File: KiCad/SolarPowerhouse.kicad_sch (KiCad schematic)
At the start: 0 parts

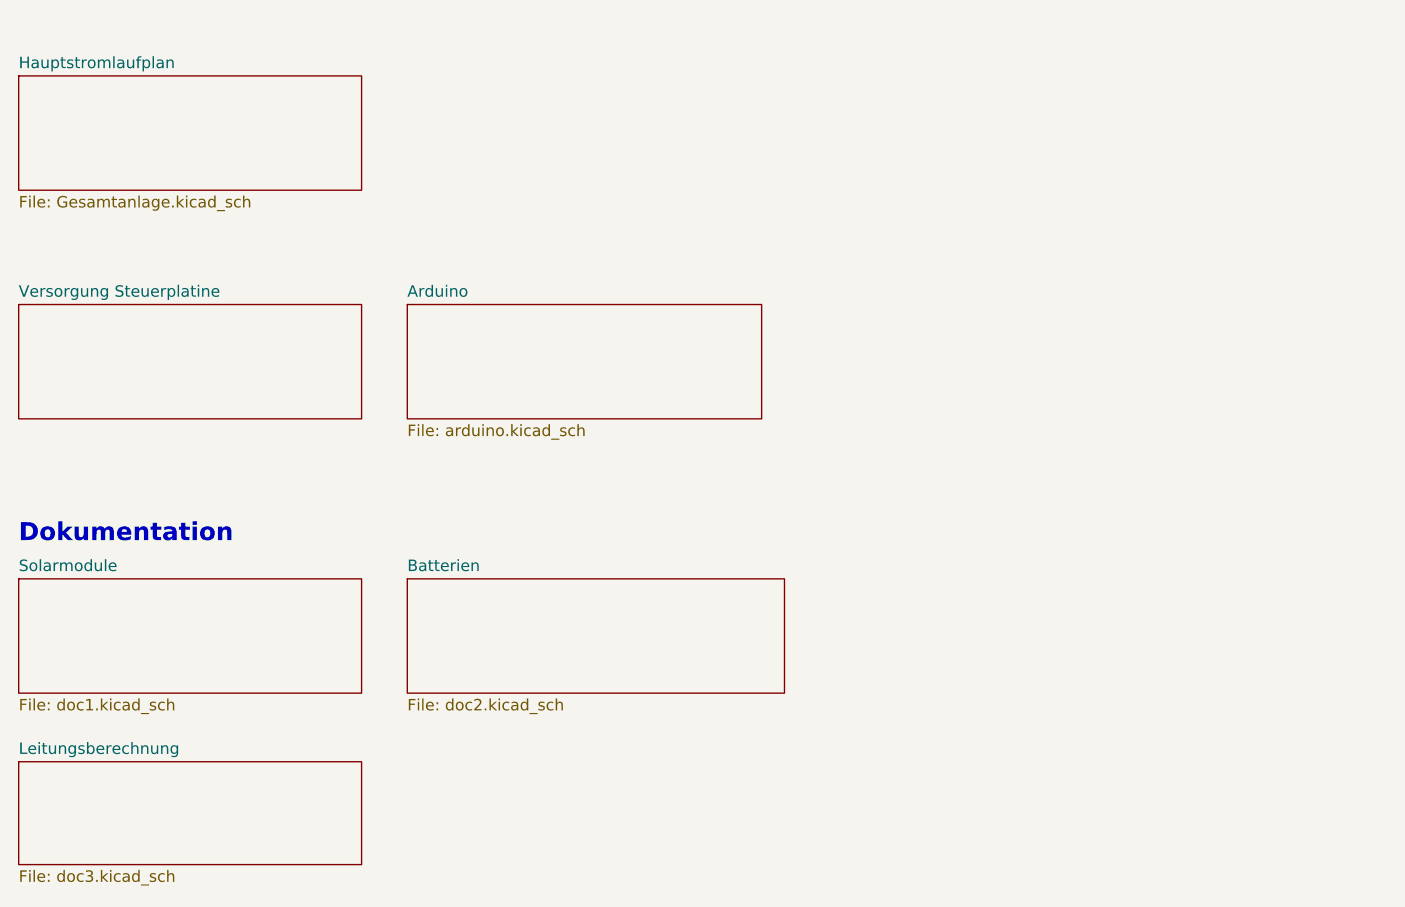
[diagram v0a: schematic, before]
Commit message: repository clean up | circuit diagram modified -> still have to add the wiring of the power supply in the circuit cabinet and the wiring of the UPS module
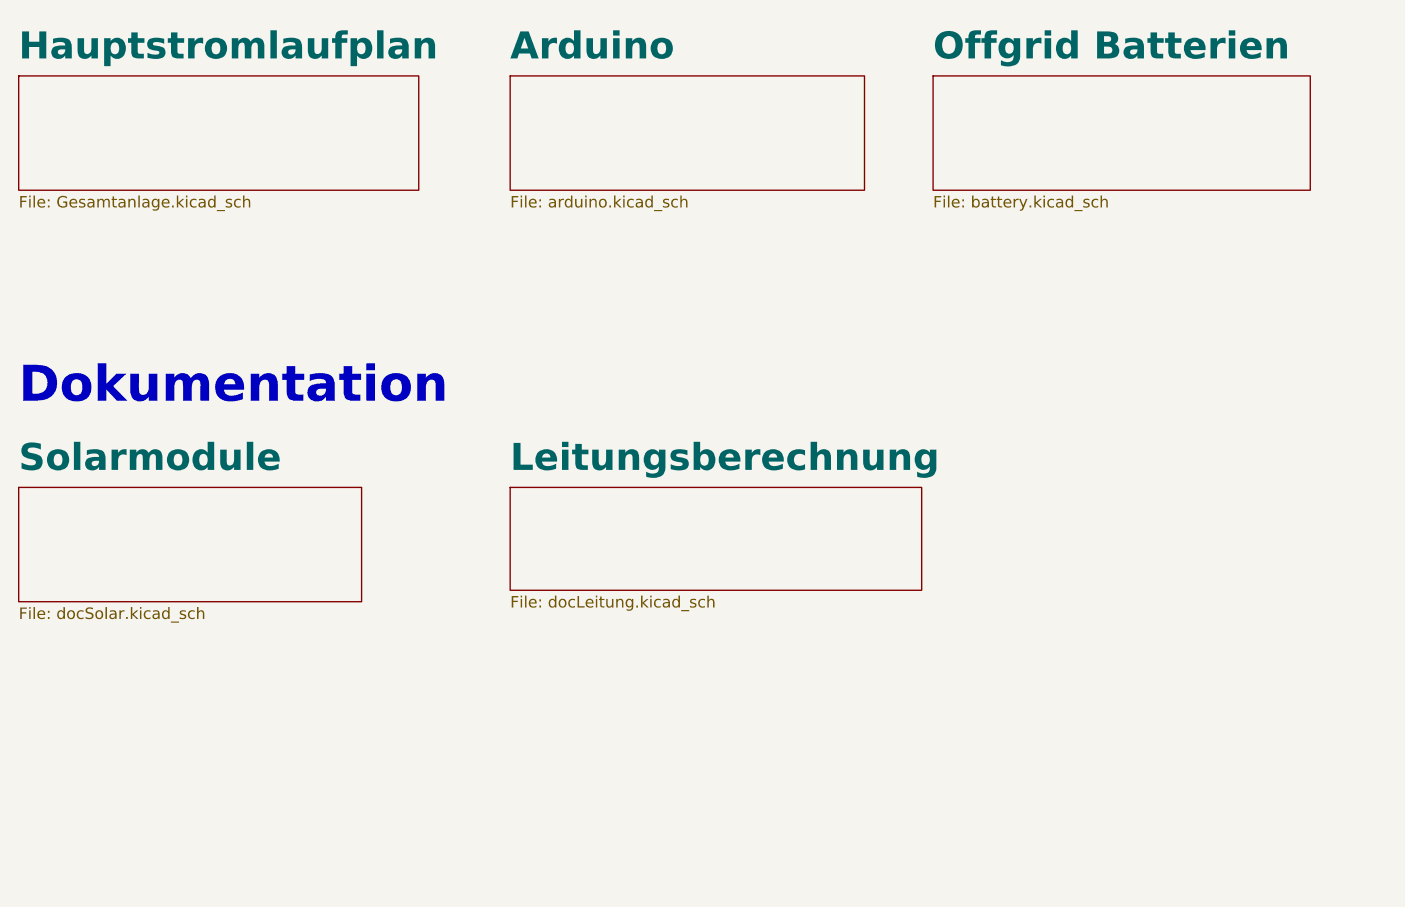
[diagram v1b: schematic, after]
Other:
- sheet Batterien renamed Offgrid Batterien
- removed sheet Versorgung Steuerplatine
- sheet Leitungsberechnung: file doc3.kicad_sch -> docLeitung.kicad_sch
- sheet Offgrid Batterien: file doc2.kicad_sch -> battery.kicad_sch
- sheet Solarmodule: file doc1.kicad_sch -> docSolar.kicad_sch
- title: (none) -> Deckblatt
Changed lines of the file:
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@@
   (paper "A4")
   (title_block
-    (date "2023-06-27")
-    (rev "1.1")
+    (title "Deckblatt")
+    (date "2024-02-03")
+    (rev "1.2")
   )
-  (text "Dokumentation" (at 25.4 82.55 0)
-    (effects (font (size 2 2) (thickness 0.4) bold) (justify left bottom))
+  (text "Dokumentation" (at 25.4 67.31 0)
+    (effects (font (size 4 4) (thickness 0.4) bold) (justify left bottom))
   )
-  (sheet (at 25.4 55.88) (size 38.1 12.7) (fields_autoplaced)
+  (sheet (at 80.01 30.48) (size 39.37 12.7) (fields_autoplaced)
     (stroke (width 0.1524) (type solid))
     (fill (color 0 0 0 0.0000))
-    (property "Sheetname" "Versorgung Steuerplatine" (at 25.4 55.1684 0)
-      (effects (font (size 1.27 1.27)) (justify left bottom))
+    (property "Sheetname" "Arduino" (at 80.01 28.9034 0)
+      (effects (font (size 3 3) bold) (justify left bottom))
     )
-    (property "Sheetfile" "powerSupply.kicad_sch" (at 25.4 69.1646 0)
-      (effects (font (size 1.27 1.27)) (justify left top) hide)
+    (property "Sheetfile" "arduino.kicad_sch" (at 80.01 43.7646 0)
+      (effects (font (size 1.27 1.27)) (justify left top))
     )
     (instances
@@
     )
   )
-  (sheet (at 68.58 55.88) (size 39.37 12.7) (fields_autoplaced)
+  (sheet (at 80.01 76.2) (size 45.72 11.43) (fields_autoplaced)
     (stroke (width 0.1524) (type solid))
     (fill (color 0 0 0 0.0000))
-    (property "Sheetname" "Arduino" (at 68.58 55.1684 0)
-      (effects (font (size 1.27 1.27)) (justify left bottom))
+    (property "Sheetname" "Leitungsberechnung" (at 80.01 74.6234 0)
+      (effects (font (size 3 3) bold) (justify left bottom))
     )
-    (property "Sheetfile" "arduino.kicad_sch" (at 68.58 69.1646 0)
-      (effects (font (size 1.27 1.27)) (justify left top))
-    )
-    (instances
-      (project "SolarPowerhouse"
-        (path "/3df9bc04-15ae-4584-9deb-0b3953389171" (page "6"))
-      )
-    )
-  )
-  (sheet (at 25.4 106.68) (size 38.1 11.43) (fields_autoplaced)
-    (stroke (width 0.1524) (type solid))
-    (fill (color 0 0 0 0.0000))
-    (property "Sheetname" "Leitungsberechnung" (at 25.4 105.9684 0)
-      (effects (font (size 1.27 1.27)) (justify left bottom))
-    )
-    (property "Sheetfile" "doc3.kicad_sch" (at 25.4 118.6946 0)
+    (property "Sheetfile" "docLeitung.kicad_sch" (at 80.01 88.2146 0)
       (effects (font (size 1.27 1.27)) (justify left top))
     )
@@
     )
   )
-  (sheet (at 25.4 86.36) (size 38.1 12.7) (fields_autoplaced)
+  (sheet (at 25.4 76.2) (size 38.1 12.7) (fields_autoplaced)
     (stroke (width 0.1524) (type solid))
     (fill (color 0 0 0 0.0000))
-    (property "Sheetname" "Solarmodule" (at 25.4 85.6484 0)
-      (effects (font (size 1.27 1.27)) (justify left bottom))
+    (property "Sheetname" "Solarmodule" (at 25.4 74.6234 0)
+      (effects (font (size 3 3) bold) (justify left bottom))
     )
-    (property "Sheetfile" "doc1.kicad_sch" (at 25.4 99.6446 0)
+    (property "Sheetfile" "docSolar.kicad_sch" (at 25.4 89.4846 0)
+      (effects (font (size 1.27 1.27)) (justify left top))
+    )
+    (instances
+      (project "SolarPowerhouse"
+        (path "/3df9bc04-15ae-4584-9deb-0b3953389171" (page "5"))
+      )
+    )
+  )
+  (sheet (at 127 30.48) (size 41.91 12.7) (fields_autoplaced)
+    (stroke (width 0.1524) (type solid))
+    (fill (color 0 0 0 0.0000))
+    (property "Sheetname" "Offgrid Batterien" (at 127 28.9034 0)
+      (effects (font (size 3 3) bold) (justify left bottom))
+    )
+    (property "Sheetfile" "battery.kicad_sch" (at 127 43.7646 0)
       (effects (font (size 1.27 1.27)) (justify left top))
     )
@@
     )
   )
-  (sheet (at 68.58 86.36) (size 41.91 12.7) (fields_autoplaced)
+  (sheet (at 25.4 30.48) (size 44.45 12.7) (fields_autoplaced)
     (stroke (width 0.1524) (type solid))
     (fill (color 0 0 0 0.0000))
-    (property "Sheetname" "Batterien" (at 68.58 85.6484 0)
-      (effects (font (size 1.27 1.27)) (justify left bottom))
-    )
-    (property "Sheetfile" "doc2.kicad_sch" (at 68.58 99.6446 0)
-      (effects (font (size 1.27 1.27)) (justify left top))
-    )
-    (instances
-      (project "SolarPowerhouse"
-        (path "/3df9bc04-15ae-4584-9deb-0b3953389171" (page "5"))
-      )
-    )
-  )
-  (sheet (at 25.4 30.48) (size 38.1 12.7) (fields_autoplaced)
-    (stroke (width 0.1524) (type solid))
-    (fill (color 0 0 0 0.0000))
-    (property "Sheetname" "Hauptstromlaufplan" (at 25.4 29.7684 0)
-      (effects (font (size 1.27 1.27)) (justify left bottom))
+    (property "Sheetname" "Hauptstromlaufplan" (at 25.4 28.9034 0)
+      (effects (font (size 3 3) bold) (justify left bottom))
     )
     (property "Sheetfile" "Gesamtanlage.kicad_sch" (at 25.4 43.7646 0)
@@
   )
   (sheet_instances
-    (path "/" (page "1"))
+    (path "/" (page "5"))
   )
 )
